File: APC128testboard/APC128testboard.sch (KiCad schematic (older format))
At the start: 68 parts, among them CON1 BARREL_JACK, J1 CONN-SCSI68, K1 AMP_PWR, K2 LEMO+, K3 LEMO-, P1 SPYPAD, P10 SPYPAD, P11 SPYPAD, P12 SPYPAD, P13 SPYPAD, P14 SPYPAD, P15 SPYPAD, P16 SPYPAD, P17 SPYPAD, P18 SPYPAD, P2 MAXV_CONNA, P21 SPYPAD, P28 SPYPAD, P29 SPYPAD, P3 SPYPAD, P30 SPYPAD, P4 SPYPAD, P5 SPYPAD, P6 SPYPAD, P7 SPYPAD, P8 SPYPAD, P9 SPYPAD, U1 APC128, U2 AD8131, U3 ADP2108, U4 AD5334, U5 MAX1719

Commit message: Update to proposal 5
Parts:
- removed C2, C3: .1uF, symbol C
- removed C4, C5: 10uF, symbol C
- removed U2: AD8131, symbol AD8131
- added P19: SPYPAD, SCSI:testpad, symbol SPYPAD
- added R13: ?, SMD_Packages:SM0603_Resistor, symbol R
- C1, R10, R11, R12: footprint (none) -> SMD_Packages:SM0603
- C6, C7, C8, C9: footprint (none) -> SMD_Packages:SM0603_Capa
- CON1: footprint (none) -> Connect:BARREL_JACK
- J1: footprint (none) -> SCSI:SCSI68up
- JP1, JP2, JP3, JP4, JP5, JP6, JP7, K1: footprint (none) -> Connect:SIL-3
- K2, K3: footprint (none) -> extras:LEMO_EPL.00.250.NTN
- L1: footprint (none) -> extras:SMD_1008
- P1, P10, P11, P12, P13, P14, P15, P16, P17, P18, P21, P28, P29, P3, P30, P4, P5, P6, P7, P8, P9: footprint (none) -> SCSI:testpad
- P2: footprint (none) -> Pin_Headers:Pin_Header_Straight_2x20
- R1, R33, R34, R6, R7, R8, R9: footprint (none) -> SMD_Packages:SM0603_Resistor
- RP1, RP2, RP3, RP4: footprint (none) -> extras:R8_MNR18
- RV1, RV2, RV3, RV4, RV5: footprint (none) -> extras:Pot-Bourns3310Y
- U1: footprint (none) -> APC128:APC128
- U3: footprint (none) -> SMD_Packages:SOT23-5
- U4: footprint MODULE -> TSSOP:TSSOP24
- U5: footprint MODULE -> SMD_Packages:SOT23_6
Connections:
- net labels added: OUT+, OUT-
- net labels removed: +OUT, -OUT, DTB_OUT+, DTB_OUT-
- wire segments 271 -> 259
- no-connect marks 15 -> 14
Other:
- note removed: "Fast amplifier\nGain: x2"
- moved on the sheet: C1, JP7, K2, K3, P29, P30, R1, R6, R8, R9

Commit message: Final touchups for APC128testboard submission.
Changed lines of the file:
@@
 Text Notes 8800 3350 3    60   ~ 0
 Connect to Max V Eval-board\nDigikey: DK-DEV-5M570ZN
-Text Notes 1200 3950 0    60   ~ 0
+Text Notes 950  4100 0    60   ~ 0
 Select Pot or DAC as \nanalog sources for APC
 Text Notes 2550 5950 0    60   ~ 0
@@
 U 539B5033
 F0 "Amplifier Stage" 60
-F1 "APC128Testboard_ampstage.sch" 60
+F1 "APC128testboard_ampstage.sch" 60
 F2 "GND" I L 2400 1700 60
 F3 "OUT+" O R 3450 1350 60

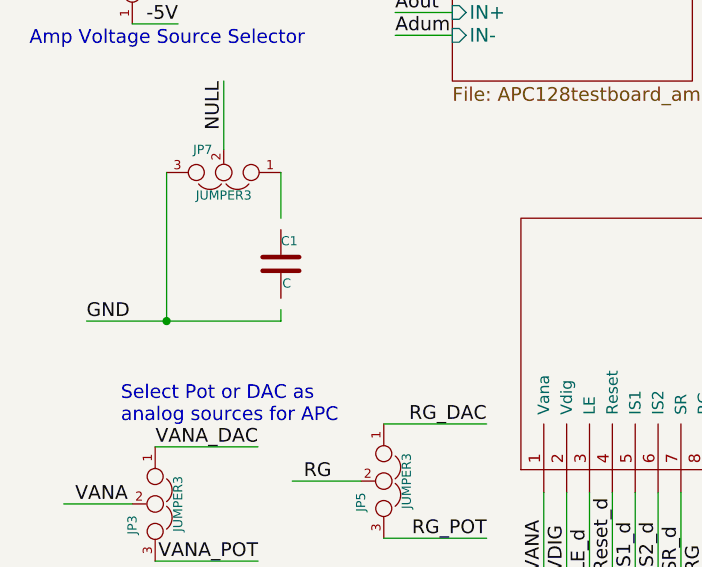
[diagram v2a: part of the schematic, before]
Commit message: Updated some passive values based on what is actually on the board.
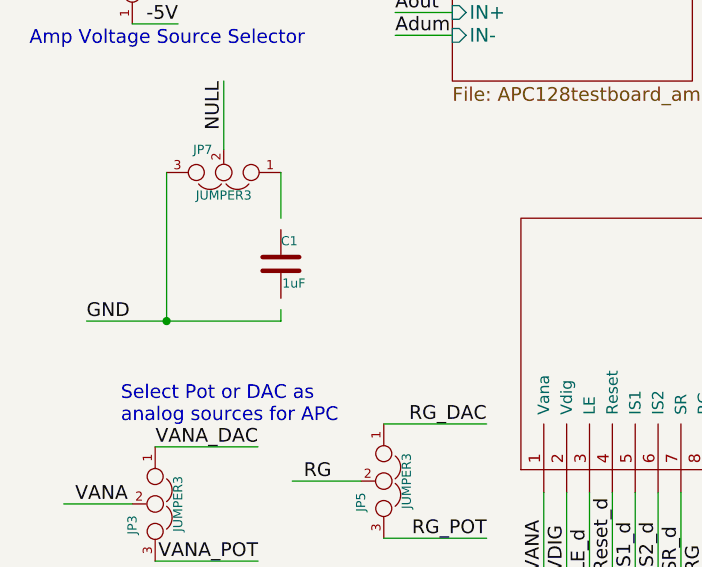
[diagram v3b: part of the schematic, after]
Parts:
- C1: value C -> 1uF
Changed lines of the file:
@@
 P 1650 3400
 F 0 "C1" H 1650 3500 40  0000 L CNN
-F 1 "C" H 1656 3315 40  0000 L CNN
+F 1 "1uF" H 1656 3315 40  0000 L CNN
 F 2 "SMD_Packages:SM0603" H 1688 3250 30  0001 C CNN
 F 3 "" H 1650 3400 60  0000 C CNN

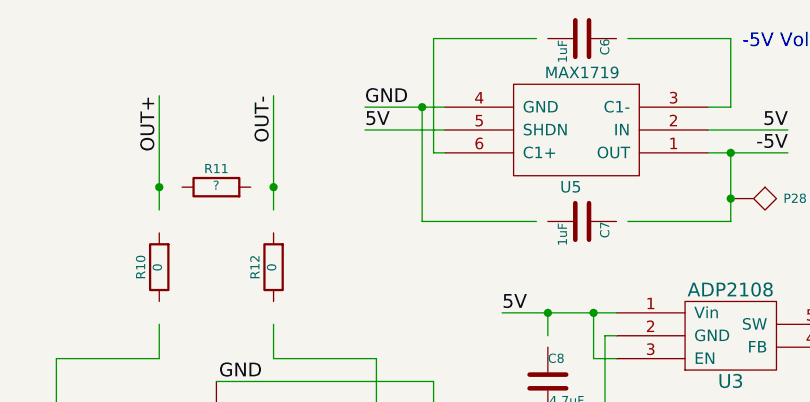
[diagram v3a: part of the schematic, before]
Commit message: Fixed incorrect polarity on -5V regulator shutdown pin. Fix is only for reference. This change is *not* on the board.
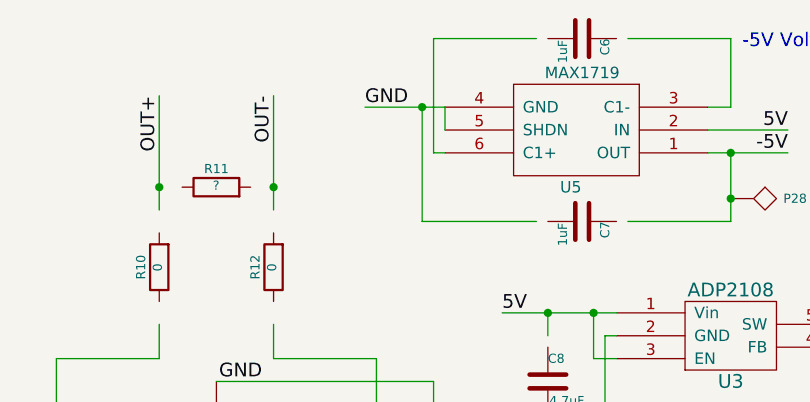
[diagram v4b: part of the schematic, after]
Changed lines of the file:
@@
 Text Label 7850 950  0    60   ~ 0
 GND
-Text Label 7850 1050 0    60   ~ 0
-5V
 Text Label 9700 1050 2    60   ~ 0
 5V
@@
 	7850 950  8200 950
 Wire Wire Line
-	8200 1050 7850 1050
-Wire Wire Line
 	8150 1150 8200 1150
 Wire Wire Line
@@
 Connection ~ 3850 1350
 Connection ~ 3850 1250
+Wire Wire Line
+	8200 950  8200 1050
 $EndSCHEMATC

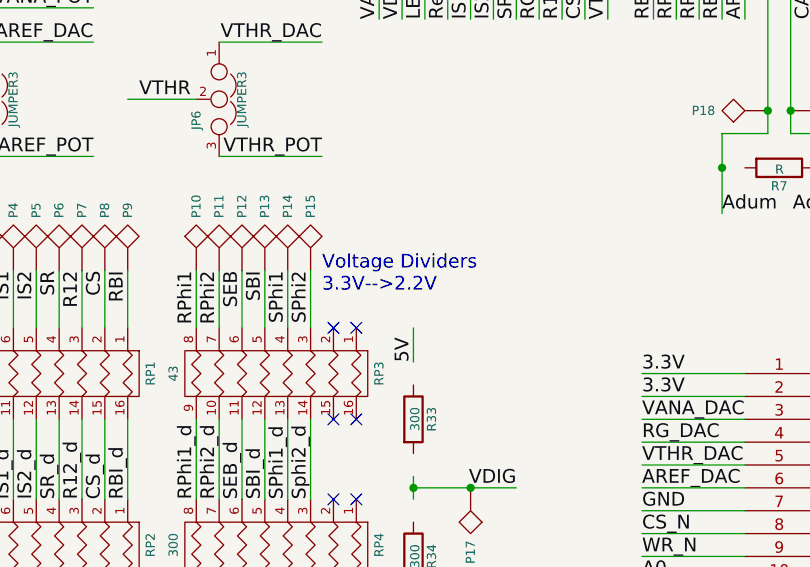
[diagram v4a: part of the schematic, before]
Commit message: Changed text for the signal voltage dividers. They actually reduce 3.3V to ~2.9V. This was a mistake. However, the 2.9V levels seem to be working ok.
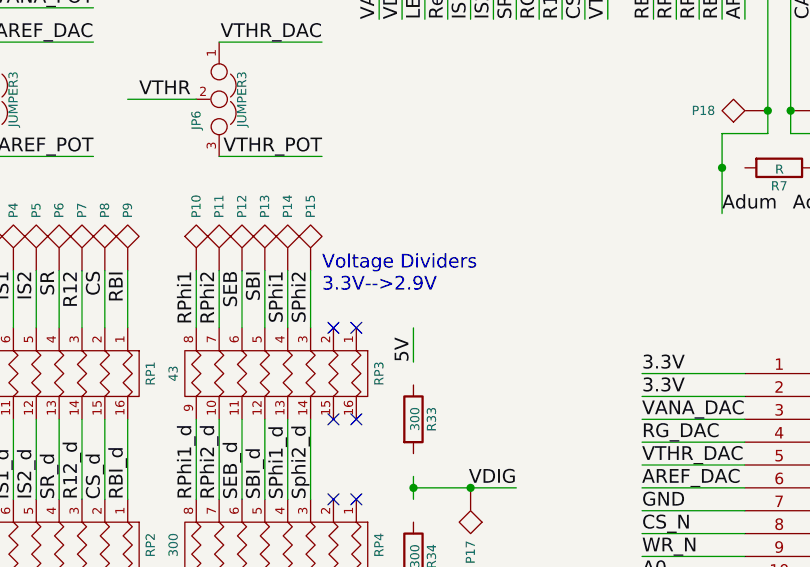
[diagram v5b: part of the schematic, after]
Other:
- note added: "Voltage Dividers \n3.3V-->2.9V"
- note removed: "Voltage Dividers \n3.3V-->2.2V"
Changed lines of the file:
@@
 Select Pot or DAC as \nanalog sources for APC
 Text Notes 2550 5950 0    60   ~ 0
-Voltage Dividers \n3.3V-->2.2V
+Voltage Dividers \n3.3V-->2.9V
 Text Notes 4700 6050 0    60   ~ 0
 DAC for setting some \nanalog levels

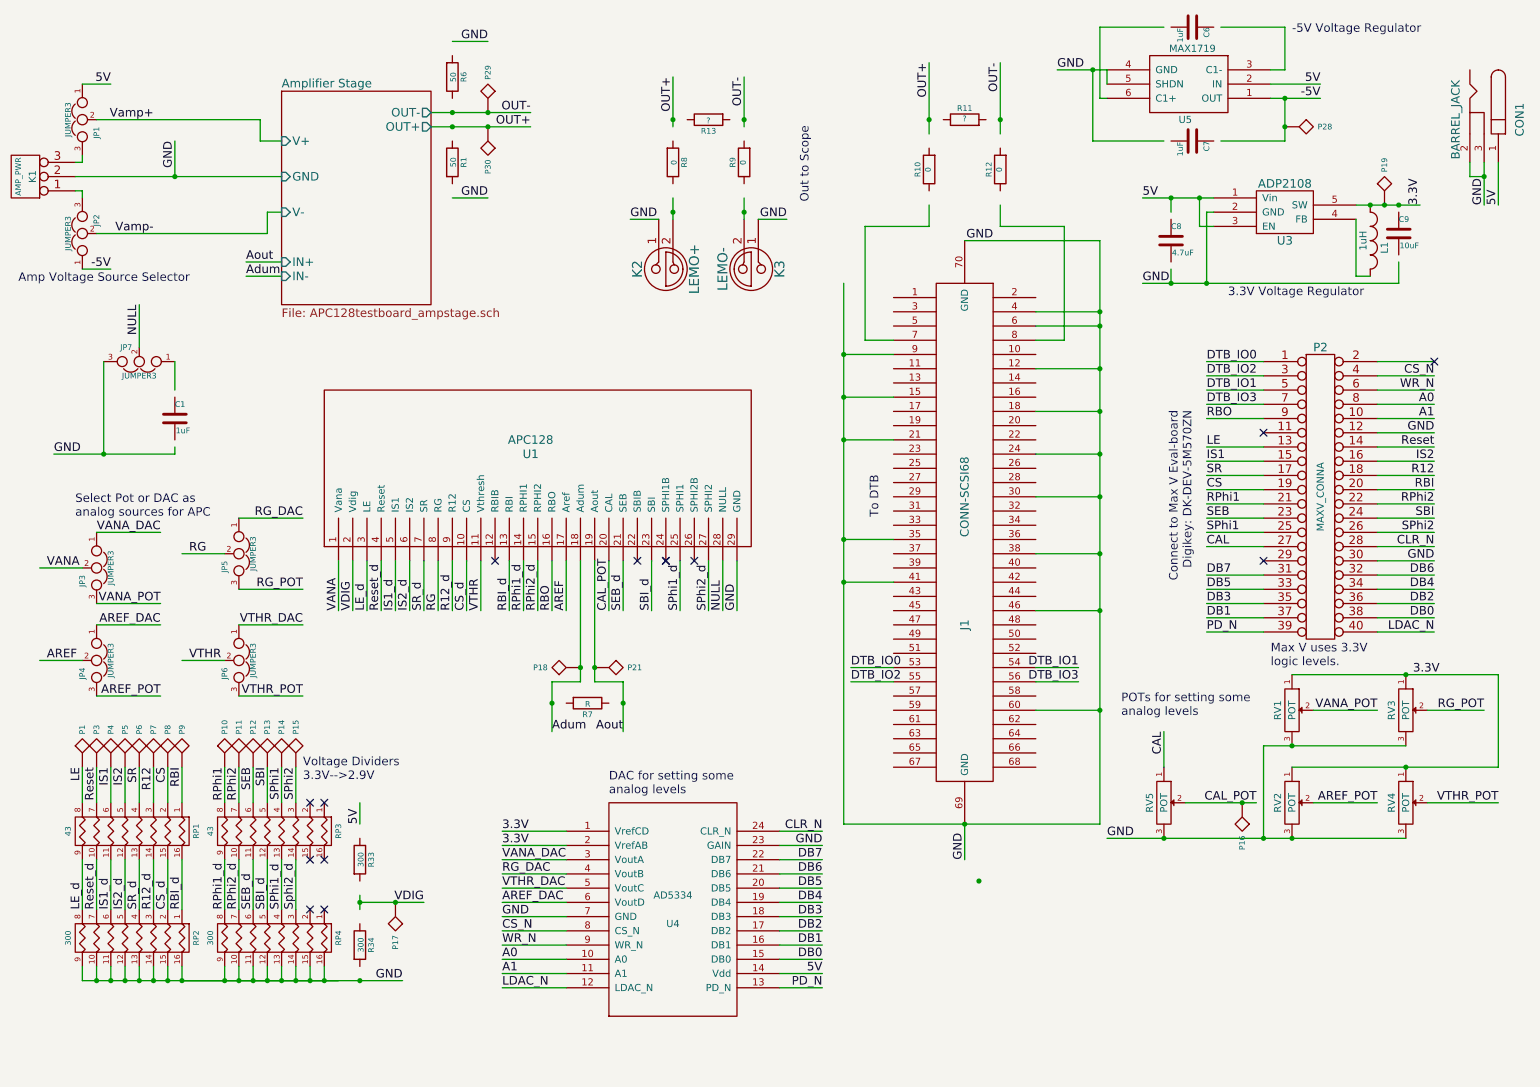
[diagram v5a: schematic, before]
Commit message: fixes broken passives in APC128 testboard schematic
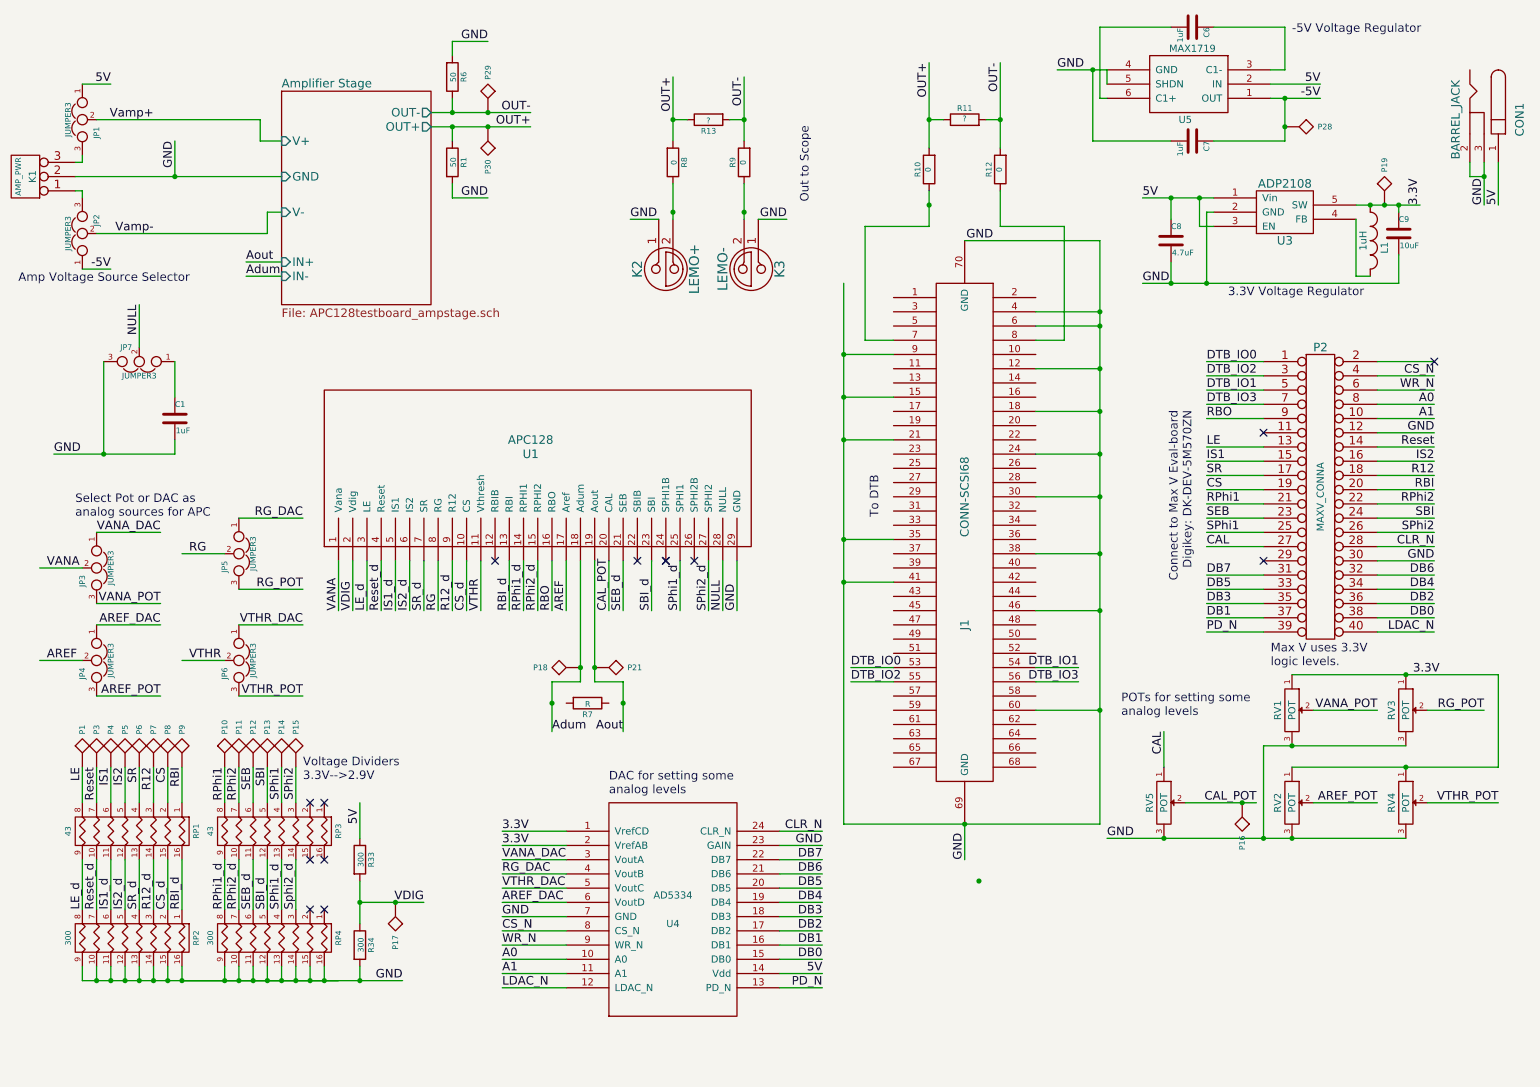
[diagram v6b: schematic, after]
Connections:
- wire segments 259 -> 269

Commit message: work on APC128 Testboard V2
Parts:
- removed C8: 4.7uF, SMD_Packages:SM0603_Capa, symbol C
- removed C9: 10uF, SMD_Packages:SM0603_Capa, symbol C
- removed J1: CONN-SCSI68, SCSI:SCSI68up, symbol CONN-SCSI68
- removed JP1, JP2, JP3, JP4, JP5, JP6, JP7: JUMPER3, Connect:SIL-3, symbol JUMPER3
- removed K1: AMP_PWR, Connect:SIL-3, symbol CONN_3
- removed K2: LEMO+, extras:LEMO_EPL.00.250.NTN, symbol LEMO2
- removed K3: LEMO-, extras:LEMO_EPL.00.250.NTN, symbol LEMO2
- removed L1: 1uH, extras:SMD_1008, symbol INDUCTOR_SMALL
- removed P18, P21, P28, P29, P30: SPYPAD, SCSI:testpad, symbol SPYPAD
- removed R1: 50, SMD_Packages:SM0603_Resistor, symbol R
- removed R10, R12: 0, SMD_Packages:SM0603, symbol R
- removed R11: ?, SMD_Packages:SM0603, symbol R
- removed R13: ?, SMD_Packages:SM0603_Resistor, symbol R
- removed R33, R34: 300, SMD_Packages:SM0603_Resistor, symbol R
- removed R8, R9: 0, SMD_Packages:SM0603_Resistor, symbol R
- removed U3: ADP2108, SMD_Packages:SOT23-5, symbol ADP2108
- removed U5: MAX1719, SMD_Packages:SOT23_6, symbol MAX1719
- added C10, C8, C9: 10uF, extras:SMD_Cap_8mmDia, symbol CP
- added C11, C3: 0.1uF, SMD_Packages:SMD-0603, symbol C
- added C2: 1000pF, SMD_Packages:SMD-0603, symbol C
- added C4, C5: 1uF, SMD_Packages:SMD-0603, symbol C
- added J1: RJ45, Connect:RJ45_8, symbol RJ45
- added JP1, JP2: JUMPER, Pin_Headers:Pin_Header_Straight_1x02, symbol JUMPER
- added JP8, JP9: JUMPER, extras:Harwin_D3082-05, symbol JUMPER
- added R1, R2: Rg, extras:SM31TW+0805, symbol RVAR
- added R3, R4: Rf, extras:SM31TW+0805, symbol RVAR
- added R5: 50R, SMD_Packages:SMD-0603, symbol R
- added RV6: POT, extras:SM31TW+0805, symbol POT
- added SW1, SW2, SW3, SW4, SW5: SWITCH_INV, extras:TE-Switch-SPDT, symbol SWITCH_INV
- added U2: ADA4932-1, extras:ADA4950-1, symbol ADA4932-1
- added U3, U5: LT1761, extras:TSOT-23-5, symbol LT1761
- C1: footprint SMD_Packages:SM0603 -> SMD_Packages:SMD-0603
- C6, C7: value 1uF -> 0.01uF; footprint SMD_Packages:SM0603_Capa -> SMD_Packages:SMD-0603
- P1, P10, P11, P12, P13, P14, P15, P16, P17, P19, P3, P4, P5, P6, P7, P8, P9: footprint SCSI:testpad -> extras:testpad
- P2: value MAXV_CONNA -> FPGA_CONN; symbol CONN_20X2 -> CONN_20X2-RESCUE-APC128testboard
- R6: value 50 -> 50R; footprint SMD_Packages:SM0603_Resistor -> SMD_Packages:SMD-0603
- R7: value R -> DNP; footprint SMD_Packages:SM0603_Resistor -> SMD_Packages:SMD-0603
- RP1, RP3: value 43 -> JMPR
- RP2, RP4: value 300 -> DNP
- RV5: footprint extras:Pot-Bourns3310Y -> extras:SM31TW+0805
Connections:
- net -5V is gone; now on net 3.3V: C7.1
- net Adum is gone; now on an unnamed net: U1.18 (Adum)
- net Aout is gone; now on an unnamed net: U1.19 (Aout)
- net VDIG is gone; now on net 2.5V: P17.1, U1.2 (Vdig)
- net 3.3V: now also C9.1, RV6.1, U5.5 (OUT)
- net 5V: now also C10.1, C11.1, C2.1, C3.1, C4.2, C5.2, U2.5 (+Vs), U2.6 (+Vs), U2.7 (+Vs), U2.8 (+Vs), U3.1 (IN), U3.3 (SHDN_N), U5.1 (IN), U5.3 (SHDN_N)
- net AREF: now also SW2.2
- net AREF_DAC: now also U4.3 (VoutA), SW2.1; no longer U4.6 (VoutD)
- net AREF_POT: now also SW2.3
- net CS: now also P2.20 (P20), P9.1, RP1.1 (P1); no longer P2.19 (P19), P8.1, RP1.2 (P2)
- net CS_d: now also RP1.16 (R1), RP2.1 (P1); no longer RP1.15 (R2), RP2.2 (P2)
- net GND: now also C10.2, C11.2, C2.2, C3.2, C4.1, C5.1, J1.9 (SHIELD), JP8.1, JP8.2, JP9.1, JP9.2, RV6.3, SW5.3, U2.0 (PAD), U2.12 (~PD), U2.13 (-Vs), U2.14 (-Vs), U2.15 (-Vs), U2.16 (-Vs), U3.2 (GND), U5.2 (GND); no longer C7.2, R6.2
- net IS1: now also P13.1, P2.24 (P24), RP3.5 (P5); no longer P2.15 (P15), P4.1, RP1.6 (P6)
- net IS1_d: now also RP3.12 (R5), RP4.5 (P5); no longer RP1.11 (R6), RP2.6 (P6)
- net IS2: now also P12.1, P2.23 (P23), RP3.6 (P6); no longer P2.16 (P16), P5.1, RP1.5 (P5)
- net IS2_d: now also RP3.11 (R6), RP4.6 (P6); no longer RP1.12 (R5), RP2.5 (P5)
- net LE: now also P15.1, P2.26 (P26), RP3.3 (P3); no longer P1.1, P2.13 (P13), RP1.8 (P8)
- net LE_d: now also RP3.14 (R3), RP4.3 (P3); no longer RP1.9 (R8), RP2.8 (P8)
- net NULL: now also SW5.2
- net R12: now also P10.1, P2.21 (P21), RP3.8 (P8); no longer P2.18 (P18), P7.1, RP1.3 (P3)
- net R12_d: now also RP3.9 (R8), RP4.8 (P8); no longer RP1.14 (R3), RP2.3 (P3)
- net RBI: now also P2.19 (P19), P8.1, RP1.2 (P2); no longer P2.20 (P20), P9.1, RP1.1 (P1)
- net RBI_d: now also RP1.15 (R2), RP2.2 (P2); no longer RP1.16 (R1), RP2.1 (P1)
- net RG: now also SW3.2
- net RG_DAC: now also U4.5 (VoutC), SW3.1; no longer U4.4 (VoutB)
- net RG_POT: now also SW3.3
- net RPhi1: now also P2.18 (P18), P7.1, RP1.3 (P3); no longer P10.1, P2.21 (P21), RP3.8 (P8)
- net RPhi1_d: now also RP1.14 (R3), RP2.3 (P3); no longer RP3.9 (R8), RP4.8 (P8)
- net RPhi2: now also P2.17 (P17), P6.1, RP1.4 (P4); no longer P11.1, P2.22 (P22), RP3.7 (P7)
- net RPhi2_d: now also RP1.13 (R4), RP2.4 (P4); no longer RP3.10 (R7), RP4.7 (P7)
- net Reset: now also P14.1, P2.25, RP3.4 (P4); no longer P2.14 (P14), P3.1, RP1.7 (P7)
- net Reset_d: now also RP3.13 (R4), RP4.4 (P4); no longer RP1.10 (R7), RP2.7 (P7)
- net SBI: now also P2.15 (P15), P4.1, RP1.6 (P6); no longer P13.1, P2.24 (P24), RP3.5 (P5)
- net SBI_d: now also RP1.11 (R6), RP2.6 (P6); no longer RP3.12 (R5), RP4.5 (P5)
- net SEB: now also P2.16 (P16), P5.1, RP1.5 (P5); no longer P12.1, P2.23 (P23), RP3.6 (P6)
- net SEB_d: now also RP1.12 (R5), RP2.5 (P5); no longer RP3.11 (R6), RP4.6 (P6)
- net SPhi1: now also P2.14 (P14), P3.1, RP1.7 (P7); no longer P14.1, P2.25, RP3.4 (P4)
- net SPhi1_d: now also RP1.10 (R7), RP2.7 (P7); no longer RP3.13 (R4), RP4.4 (P4)
- net SPhi2: now also P1.1, P2.13 (P13), RP1.8 (P8); no longer P15.1, P2.26 (P26), RP3.3 (P3)
- net SR: now also P11.1, P2.22 (P22), RP3.7 (P7); no longer P2.17 (P17), P6.1, RP1.4 (P4)
- net SR_d: now also RP3.10 (R7), RP4.7 (P7); no longer RP1.13 (R4), RP2.4 (P4)
- net Sphi2_d: now also RP1.9 (R8), RP2.8 (P8); no longer RP3.14 (R3), RP4.3 (P3)
- net VANA: now also SW1.2
- net VANA_DAC: now also U4.6 (VoutD), SW1.1; no longer U4.3 (VoutA)
- net VANA_POT: now also SW1.3
- net VTHR: now also SW4.2
- net VTHR_DAC: now also U4.4 (VoutB), SW4.1; no longer U4.5 (VoutC)
- net VTHR_POT: now also SW4.3
- net 2.5V: now reaches C6.1
- net 2.5V: now also C8.1, U3.5 (OUT)
- net at C6.2: now also C8.2, U3.4 (BYP)
- net at R7.1: now also JP2.1
- net at R7.2: now also JP1.1
- net at C1.1: now also SW5.1
- net DTB_IO0: no longer names the net of P2.1 (P1)
- net DTB_IO1: no longer names the net of P2.5 (P5)
- net DTB_IO2: no longer names the net of P2.3 (P3)
- net DTB_IO3: no longer names the net of P2.7 (P7)
- net OUT-: no longer names the net of R6.1
- net OUT-: now also J1.2
- new net: JP1.2, R2.2
- new net: JP2.2, R1.2
- new net: C7.2, C9.2, U5.4 (BYP)
- new net: R3.2, U2.1 (-FB)
- new net: R6.2, U2.10 (+OUT)
- new net: R5.2, U2.11 (-OUT)
- new net: R1.1, R3.1, U2.2 (+IN)
- new net: R2.1, R4.2, U2.3 (-IN)
- new net: R4.1, U2.4 (+FB)
- new net: J1.1, R5.1
- new net AMP_OCM: RV6.2, U2.9 (Vocm)
- no-connect marks 14 -> 24
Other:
- note added: "2.5V Voltage Regulator"
- note added: "20k 5-turn POTS"
- note added: "FPGA Board uses 2.5V\nlogic levels."
- note added: "Gain=Rf/Rg"
- note added: "Voltage Dividers \n(Only use if not using 2.5V Logic levels)"
- note removed: "-5V Voltage Regulator"
- note removed: "Amp Voltage Source Selector"
- note removed: "Connect to Max V Eval-board\nDigikey: DK-DEV-5M570ZN"
- note removed: "Max V uses 3.3V\nlogic levels."
- note removed: "Out to Scope"
- note removed: "To DTB"
- note removed: "Voltage Dividers \n3.3V-->2.9V"
- moved on the sheet: C1, CON1, P1, P10, P11, P12, P13, P14, P15, P16, P19, P2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
